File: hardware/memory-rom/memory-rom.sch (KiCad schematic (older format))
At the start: 26 parts, among them J1 Conn_Mem_Ext, J2 Conn_Power, U1 SST39VF040-70-4C-NHE, U2 74LVC1G86, U3 74LVC1G32, U4 74LVC1G332, U5 74LVC1G86, U6 MIC5504-3.3YM5

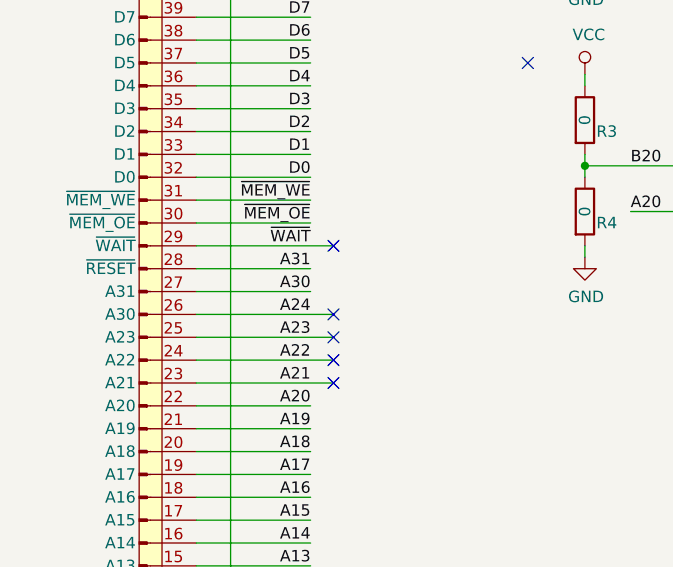
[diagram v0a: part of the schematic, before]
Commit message: Added ~RESET to memory bus
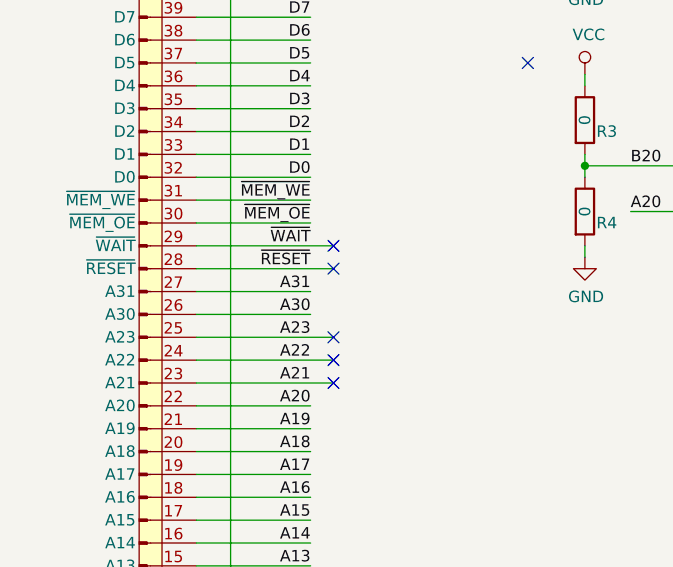
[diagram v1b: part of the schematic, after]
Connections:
- net A24 is gone; now on net A30: J1.26 (A30)
- net A30: no longer J1.27 (A31)
- net A31: now also J1.27 (A31); no longer J1.28 (~RESET)
- new net ~RESET: J1.28 (~RESET)
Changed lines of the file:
@@
 Text Label 1950 3800 2    50   ~ 0
 A23
-Text Label 1950 3700 2    50   ~ 0
-A24
 Text Label 1950 3400 2    50   ~ 0
 ~WAIT
@@
 Wire Wire Line
 	1950 4400 1450 4400
-Text Label 1950 3500 2    50   ~ 0
+Text Label 1950 3600 2    50   ~ 0
 A31
-Text Label 1950 3600 2    50   ~ 0
+Text Label 1950 3700 2    50   ~ 0
 A30
 Wire Wire Line
-	1950 3500 1450 3500
-Wire Wire Line
-	1450 3600 1950 3600
+	1950 3600 1450 3600
+Wire Wire Line
+	1450 3700 1950 3700
 $Comp
 L Mechanical:MountingHole H?
@@
 Connection ~ 1600 6200
 Wire Wire Line
-	1450 3700 2050 3700
+	1450 3500 2050 3500
 Wire Wire Line
 	1450 3800 2050 3800
@@
 Wire Wire Line
 	10100 3600 10100 3400
-NoConn ~ 2050 3700
+NoConn ~ 2050 3500
 NoConn ~ 2050 3800
 NoConn ~ 2050 3900
 NoConn ~ 2050 4000
+Text Label 1950 3500 2    50   ~ 0
+~RESET
 $EndSCHEMATC

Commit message: Unified footprints
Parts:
- D1: footprint LED_SMD:LED_0805_2012Metric -> LED_SMD:LED_0805_2012Metric_Pad1.15x1.40mm_HandSolder
- R1, R2, R3, R4, R5: footprint Resistor_SMD:R_0805_2012Metric -> Resistor_SMD:R_0805_2012Metric_Pad1.15x1.40mm_HandSolder
- U2, U3, U5, U6: footprint Package_TO_SOT_SMD:SOT-23-5 -> Package_TO_SOT_SMD:SOT-23-5_HandSoldering
- U4: footprint Package_TO_SOT_SMD:SOT-23-6 -> Package_TO_SOT_SMD:SOT-23-6_Handsoldering
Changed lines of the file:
@@
 F 0 "U4" H 6000 2333 50  0000 C CNN
 F 1 "74LVC1G332" H 6000 2424 50  0000 C CNN
-F 2 "Package_TO_SOT_SMD:SOT-23-6" H 5970 2620 50  0001 C CNN
+F 2 "Package_TO_SOT_SMD:SOT-23-6_Handsoldering" H 5970 2620 50  0001 C CNN
 F 3 "" H 5970 2620 50  0001 C CNN
 	1    6000 2650
@@
 F 0 "R1" H 3200 1500 50  0000 L CNN
 F 1 "0" V 3150 1550 50  0000 C CNN
-F 2 "Resistor_SMD:R_0805_2012Metric" V 3080 1550 50  0001 C CNN
+F 2 "Resistor_SMD:R_0805_2012Metric_Pad1.15x1.40mm_HandSolder" V 3080 1550 50  0001 C CNN
 F 3 "~" H 3150 1550 50  0001 C CNN
 	1    3150 1550
@@
 F 0 "R2" H 3200 1900 50  0000 L CNN
 F 1 "0" V 3150 1950 50  0000 C CNN
-F 2 "Resistor_SMD:R_0805_2012Metric" V 3080 1950 50  0001 C CNN
+F 2 "Resistor_SMD:R_0805_2012Metric_Pad1.15x1.40mm_HandSolder" V 3080 1950 50  0001 C CNN
 F 3 "~" H 3150 1950 50  0001 C CNN
 	1    3150 1950
@@
 F 0 "R3" H 3200 2800 50  0000 L CNN
 F 1 "0" V 3150 2850 50  0000 C CNN
-F 2 "Resistor_SMD:R_0805_2012Metric" V 3080 2850 50  0001 C CNN
+F 2 "Resistor_SMD:R_0805_2012Metric_Pad1.15x1.40mm_HandSolder" V 3080 2850 50  0001 C CNN
 F 3 "~" H 3150 2850 50  0001 C CNN
 	1    3150 2850
@@
 F 0 "R4" H 3200 3200 50  0000 L CNN
 F 1 "0" V 3150 3250 50  0000 C CNN
-F 2 "Resistor_SMD:R_0805_2012Metric" V 3080 3250 50  0001 C CNN
+F 2 "Resistor_SMD:R_0805_2012Metric_Pad1.15x1.40mm_HandSolder" V 3080 3250 50  0001 C CNN
 F 3 "~" H 3150 3250 50  0001 C CNN
 	1    3150 3250
@@
 F 0 "U3" H 4900 2875 50  0000 C CNN
 F 1 "74LVC1G32" H 4900 2784 50  0000 C CNN
-F 2 "Package_TO_SOT_SMD:SOT-23-5" H 4870 2520 50  0001 C CNN
+F 2 "Package_TO_SOT_SMD:SOT-23-5_HandSoldering" H 4870 2520 50  0001 C CNN
 F 3 "" H 4870 2520 50  0001 C CNN
 	1    4900 2550
@@
 F 0 "U5" H 3950 2833 50  0000 C CNN
 F 1 "74LVC1G86" H 3950 2924 50  0000 C CNN
-F 2 "Package_TO_SOT_SMD:SOT-23-5" H 3920 3120 50  0001 C CNN
+F 2 "Package_TO_SOT_SMD:SOT-23-5_HandSoldering" H 3920 3120 50  0001 C CNN
 F 3 "" H 3920 3120 50  0001 C CNN
 	1    3950 3150
@@
 F 0 "U2" H 3950 2175 50  0000 C CNN
 F 1 "74LVC1G86" H 3950 2084 50  0000 C CNN
-F 2 "Package_TO_SOT_SMD:SOT-23-5" H 3920 1820 50  0001 C CNN
+F 2 "Package_TO_SOT_SMD:SOT-23-5_HandSoldering" H 3920 1820 50  0001 C CNN
 F 3 "" H 3920 1820 50  0001 C CNN
 	1    3950 1850
@@
 F 0 "U6" H 7350 5967 50  0000 C CNN
 F 1 "MIC5504-3.3YM5" H 7350 5876 50  0000 C CNN
-F 2 "Package_TO_SOT_SMD:SOT-23-5" H 7350 5200 50  0001 C CNN
+F 2 "Package_TO_SOT_SMD:SOT-23-5_HandSoldering" H 7350 5200 50  0001 C CNN
 F 3 "http://ww1.microchip.com/downloads/en/DeviceDoc/MIC550X.pdf" H 7100 5850 50  0001 C CNN
 	1    7350 5600
@@
 F 0 "U2" H 3530 5846 50  0000 L CNN
 F 1 "74LVC1G86" H 3530 5755 50  0000 L CNN
-F 2 "Package_TO_SOT_SMD:SOT-23-5" H 3370 5770 50  0001 C CNN
+F 2 "Package_TO_SOT_SMD:SOT-23-5_HandSoldering" H 3370 5770 50  0001 C CNN
 F 3 "" H 3370 5770 50  0001 C CNN
 	2    3400 5800
@@
 F 0 "U5" H 4280 5846 50  0000 L CNN
 F 1 "74LVC1G86" H 4280 5755 50  0000 L CNN
-F 2 "Package_TO_SOT_SMD:SOT-23-5" H 4120 5770 50  0001 C CNN
+F 2 "Package_TO_SOT_SMD:SOT-23-5_HandSoldering" H 4120 5770 50  0001 C CNN
 F 3 "" H 4120 5770 50  0001 C CNN
 	2    4150 5800
@@
 F 0 "U3" H 5050 5900 50  0000 C CNN
 F 1 "74LVC1G32" H 5200 5800 50  0000 C CNN
-F 2 "Package_TO_SOT_SMD:SOT-23-5" H 4820 5770 50  0001 C CNN
+F 2 "Package_TO_SOT_SMD:SOT-23-5_HandSoldering" H 4820 5770 50  0001 C CNN
 F 3 "" H 4820 5770 50  0001 C CNN
 	2    4850 5800
@@
 F 0 "U4" H 2780 5846 50  0000 L CNN
 F 1 "74LVC1G332" H 2780 5755 50  0000 L CNN
-F 2 "Package_TO_SOT_SMD:SOT-23-6" H 2620 5770 50  0001 C CNN
+F 2 "Package_TO_SOT_SMD:SOT-23-6_Handsoldering" H 2620 5770 50  0001 C CNN
 F 3 "" H 2620 5770 50  0001 C CNN
 	2    2650 5800
@@
 F 0 "R5" H 10150 3200 50  0000 L CNN
 F 1 "330" V 10100 3250 50  0000 C CNN
-F 2 "Resistor_SMD:R_0805_2012Metric" V 10030 3250 50  0001 C CNN
+F 2 "Resistor_SMD:R_0805_2012Metric_Pad1.15x1.40mm_HandSolder" V 10030 3250 50  0001 C CNN
 F 3 "~" H 10100 3250 50  0001 C CNN
 	1    10100 3250
@@
 F 0 "D1" V 10138 2633 50  0000 R CNN
 F 1 "LED" V 10047 2633 50  0000 R CNN
-F 2 "LED_SMD:LED_0805_2012Metric" H 10100 2750 50  0001 C CNN
+F 2 "LED_SMD:LED_0805_2012Metric_Pad1.15x1.40mm_HandSolder" H 10100 2750 50  0001 C CNN
 F 3 "~" H 10100 2750 50  0001 C CNN
 	1    10100 2750

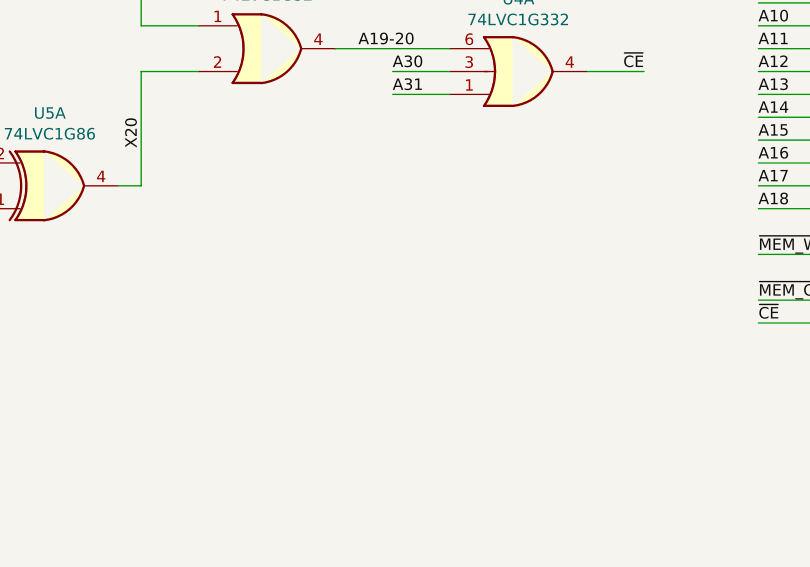
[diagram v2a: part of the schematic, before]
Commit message: Added test points
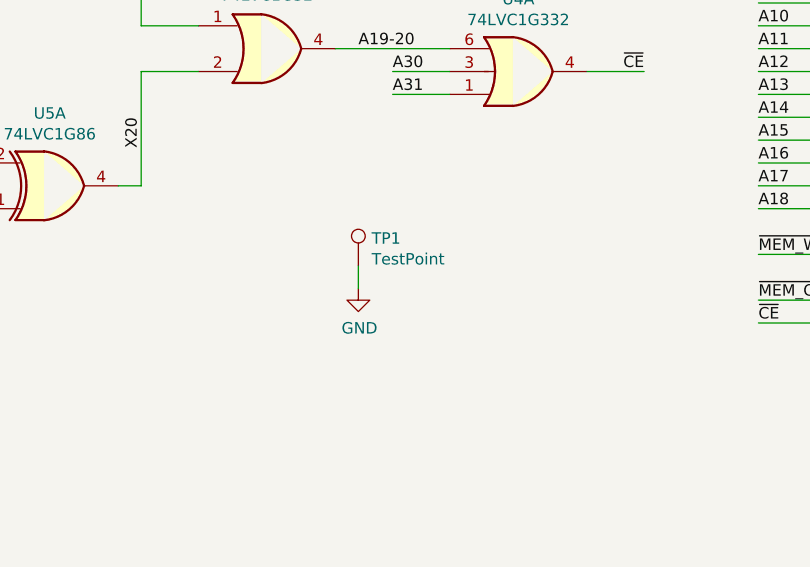
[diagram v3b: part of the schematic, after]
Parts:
- added TP1: TestPoint, TestPoint:TestPoint_THTPad_D2.0mm_Drill1.0mm, symbol Connector:TestPoint
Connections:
- net GND: now also TP1.1
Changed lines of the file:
@@
 P 8000 1150
 AR Path="/5EC6F875/5EC7A90A" Ref="#PWR?"  Part="1"
-AR Path="/5EC7A90A" Ref="#PWR01"  Part="1"
-F 0 "#PWR01" H 8000 1000 50  0001 C CNN
+AR Path="/5EC7A90A" Ref="#PWR?"  Part="1"
+F 0 "#PWR?" H 8000 1000 50  0001 C CNN
 F 1 "VCC" H 8017 1323 50  0000 C CNN
 F 2 "" H 8000 1150 50  0001 C CNN
@@
 P 8000 4050
 AR Path="/5EC6F875/5EC7A911" Ref="#PWR?"  Part="1"
-AR Path="/5EC7A911" Ref="#PWR07"  Part="1"
-F 0 "#PWR07" H 8000 3800 50  0001 C CNN
+AR Path="/5EC7A911" Ref="#PWR?"  Part="1"
+F 0 "#PWR?" H 8000 3800 50  0001 C CNN
 F 1 "GND" H 8005 3877 50  0000 C CNN
 F 2 "" H 8000 4050 50  0001 C CNN
@@
 P 1600 6300
 AR Path="/5ED0998A/5EC7A9C0" Ref="#PWR?"  Part="1"
-AR Path="/5EC7A9C0" Ref="#PWR012"  Part="1"
+AR Path="/5EC7A9C0" Ref="#PWR?"  Part="1"
 AR Path="/5EC6F875/5EC7A9C0" Ref="#PWR?"  Part="1"
-F 0 "#PWR012" H 1600 6050 50  0001 C CNN
+F 0 "#PWR?" H 1600 6050 50  0001 C CNN
 F 1 "GND" H 1605 6127 50  0000 C CNN
 F 2 "" H 1600 6300 50  0001 C CNN
@@
 P 3150 2150
 AR Path="/5EF37502/5EF44DEB" Ref="#PWR?"  Part="1"
-AR Path="/5EF44DEB" Ref="#PWR03"  Part="1"
-F 0 "#PWR03" H 3150 1900 50  0001 C CNN
+AR Path="/5EF44DEB" Ref="#PWR?"  Part="1"
+F 0 "#PWR?" H 3150 1900 50  0001 C CNN
 F 1 "GND" H 3155 1977 50  0000 C CNN
 F 2 "" H 3150 2150 50  0001 C CNN
@@
 P 3150 1350
 AR Path="/5EF37502/5EF44DF2" Ref="#PWR?"  Part="1"
-AR Path="/5EF44DF2" Ref="#PWR02"  Part="1"
-F 0 "#PWR02" H 3150 1200 50  0001 C CNN
+AR Path="/5EF44DF2" Ref="#PWR?"  Part="1"
+F 0 "#PWR?" H 3150 1200 50  0001 C CNN
 F 1 "VCC" H 3167 1523 50  0000 C CNN
 F 2 "" H 3150 1350 50  0001 C CNN
@@
 P 3150 3450
 AR Path="/5EF37502/5EF44E0D" Ref="#PWR?"  Part="1"
-AR Path="/5EF44E0D" Ref="#PWR06"  Part="1"
-F 0 "#PWR06" H 3150 3200 50  0001 C CNN
+AR Path="/5EF44E0D" Ref="#PWR?"  Part="1"
+F 0 "#PWR?" H 3150 3200 50  0001 C CNN
 F 1 "GND" H 3155 3277 50  0000 C CNN
 F 2 "" H 3150 3450 50  0001 C CNN
@@
 P 3150 2650
 AR Path="/5EF37502/5EF44E14" Ref="#PWR?"  Part="1"
-AR Path="/5EF44E14" Ref="#PWR05"  Part="1"
-F 0 "#PWR05" H 3150 2500 50  0001 C CNN
+AR Path="/5EF44E14" Ref="#PWR?"  Part="1"
+F 0 "#PWR?" H 3150 2500 50  0001 C CNN
 F 1 "VCC" H 3167 2823 50  0000 C CNN
 F 2 "" H 3150 2650 50  0001 C CNN
@@
 P 7900 5450
 AR Path="/5ED0998A/5EF4BF68" Ref="#PWR?"  Part="1"
-AR Path="/5EF4BF68" Ref="#PWR09"  Part="1"
+AR Path="/5EF4BF68" Ref="#PWR?"  Part="1"
 AR Path="/5EF37502/5EF4BF68" Ref="#PWR?"  Part="1"
-F 0 "#PWR09" H 7900 5300 50  0001 C CNN
+F 0 "#PWR?" H 7900 5300 50  0001 C CNN
 F 1 "VCC" H 7917 5623 50  0000 C CNN
 F 2 "" H 7900 5450 50  0001 C CNN
@@
 P 6150 6100
 AR Path="/5ED0998A/5EF4BF70" Ref="#PWR?"  Part="1"
-AR Path="/5EF4BF70" Ref="#PWR010"  Part="1"
+AR Path="/5EF4BF70" Ref="#PWR?"  Part="1"
 AR Path="/5EF37502/5EF4BF70" Ref="#PWR?"  Part="1"
-F 0 "#PWR010" H 6150 5850 50  0001 C CNN
+F 0 "#PWR?" H 6150 5850 50  0001 C CNN
 F 1 "GND" H 6155 5927 50  0000 C CNN
 F 2 "" H 6150 6100 50  0001 C CNN
@@
 P 7350 6100
 AR Path="/5ED0998A/5EF4BF87" Ref="#PWR?"  Part="1"
-AR Path="/5EF4BF87" Ref="#PWR011"  Part="1"
+AR Path="/5EF4BF87" Ref="#PWR?"  Part="1"
 AR Path="/5EF37502/5EF4BF87" Ref="#PWR?"  Part="1"
-F 0 "#PWR011" H 7350 5850 50  0001 C CNN
+F 0 "#PWR?" H 7350 5850 50  0001 C CNN
 F 1 "GND" H 7355 5927 50  0000 C CNN
 F 2 "" H 7350 6100 50  0001 C CNN
@@
 P 2650 6450
 AR Path="/5ED0998A/5EF4BFE0" Ref="#PWR?"  Part="1"
-AR Path="/5EF4BFE0" Ref="#PWR013"  Part="1"
+AR Path="/5EF4BFE0" Ref="#PWR?"  Part="1"
 AR Path="/5EF37502/5EF4BFE0" Ref="#PWR?"  Part="1"
-F 0 "#PWR013" H 2650 6200 50  0001 C CNN
+F 0 "#PWR?" H 2650 6200 50  0001 C CNN
 F 1 "GND" H 2655 6277 50  0000 C CNN
 F 2 "" H 2650 6450 50  0001 C CNN
@@
 P 2650 5150
 AR Path="/5ED0998A/5EF4BFE8" Ref="#PWR?"  Part="1"
-AR Path="/5EF4BFE8" Ref="#PWR08"  Part="1"
+AR Path="/5EF4BFE8" Ref="#PWR?"  Part="1"
 AR Path="/5EF37502/5EF4BFE8" Ref="#PWR?"  Part="1"
-F 0 "#PWR08" H 2650 5000 50  0001 C CNN
+F 0 "#PWR?" H 2650 5000 50  0001 C CNN
 F 1 "VCC" H 2667 5323 50  0000 C CNN
 F 2 "" H 2650 5150 50  0001 C CNN
@@
 P 6550 6100
 AR Path="/5EF37502/5EF4C00A" Ref="#FLG?"  Part="1"
-AR Path="/5EF4C00A" Ref="#FLG02"  Part="1"
-F 0 "#FLG02" H 6550 6175 50  0001 C CNN
+AR Path="/5EF4C00A" Ref="#FLG?"  Part="1"
+F 0 "#FLG?" H 6550 6175 50  0001 C CNN
 F 1 "PWR_FLAG" H 6550 6273 50  0000 C CNN
 F 2 "" H 6550 6100 50  0001 C CNN
@@
 P 6550 5400
 AR Path="/5EF37502/5EF4C013" Ref="#FLG?"  Part="1"
-AR Path="/5EF4C013" Ref="#FLG01"  Part="1"
-F 0 "#FLG01" H 6550 5475 50  0001 C CNN
+AR Path="/5EF4C013" Ref="#FLG?"  Part="1"
+F 0 "#FLG?" H 6550 5475 50  0001 C CNN
 F 1 "PWR_FLAG" H 6550 5574 50  0000 C CNN
 F 2 "" H 6550 5400 50  0001 C CNN
@@
 P 10100 2500
 AR Path="/5EF37502/5EF8DDFD" Ref="#PWR?"  Part="1"
-AR Path="/5EF8DDFD" Ref="#PWR04"  Part="1"
-F 0 "#PWR04" H 10100 2350 50  0001 C CNN
+AR Path="/5EF8DDFD" Ref="#PWR?"  Part="1"
+F 0 "#PWR?" H 10100 2350 50  0001 C CNN
 F 1 "VCC" H 10117 2673 50  0000 C CNN
 F 2 "" H 10100 2500 50  0001 C CNN
@@
 Text Label 1950 3500 2    50   ~ 0
 ~RESET
+$Comp
+L Connector:TestPoint TP1
+U 1 1 5F064DFA
+P 5300 3500
+F 0 "TP1" H 5358 3620 50  0000 L CNN
+F 1 "TestPoint" H 5358 3529 50  0000 L CNN
+F 2 "TestPoint:TestPoint_THTPad_D2.0mm_Drill1.0mm" H 5500 3500 50  0001 C CNN
+F 3 "~" H 5500 3500 50  0001 C CNN
+	1    5300 3500
+	1    0    0    -1
+$EndComp
+$Comp
+L power:GND #PWR?
+U 1 1 5F064E5C
+P 5300 3600
+AR Path="/5EC6F875/5F064E5C" Ref="#PWR?"  Part="1"
+AR Path="/5F064E5C" Ref="#PWR?"  Part="1"
+F 0 "#PWR?" H 5300 3350 50  0001 C CNN
+F 1 "GND" H 5305 3427 50  0000 C CNN
+F 2 "" H 5300 3600 50  0001 C CNN
+F 3 "" H 5300 3600 50  0001 C CNN
+	1    5300 3600
+	1    0    0    -1
+$EndComp
+Wire Wire Line
+	5300 3500 5300 3600
 $EndSCHEMATC

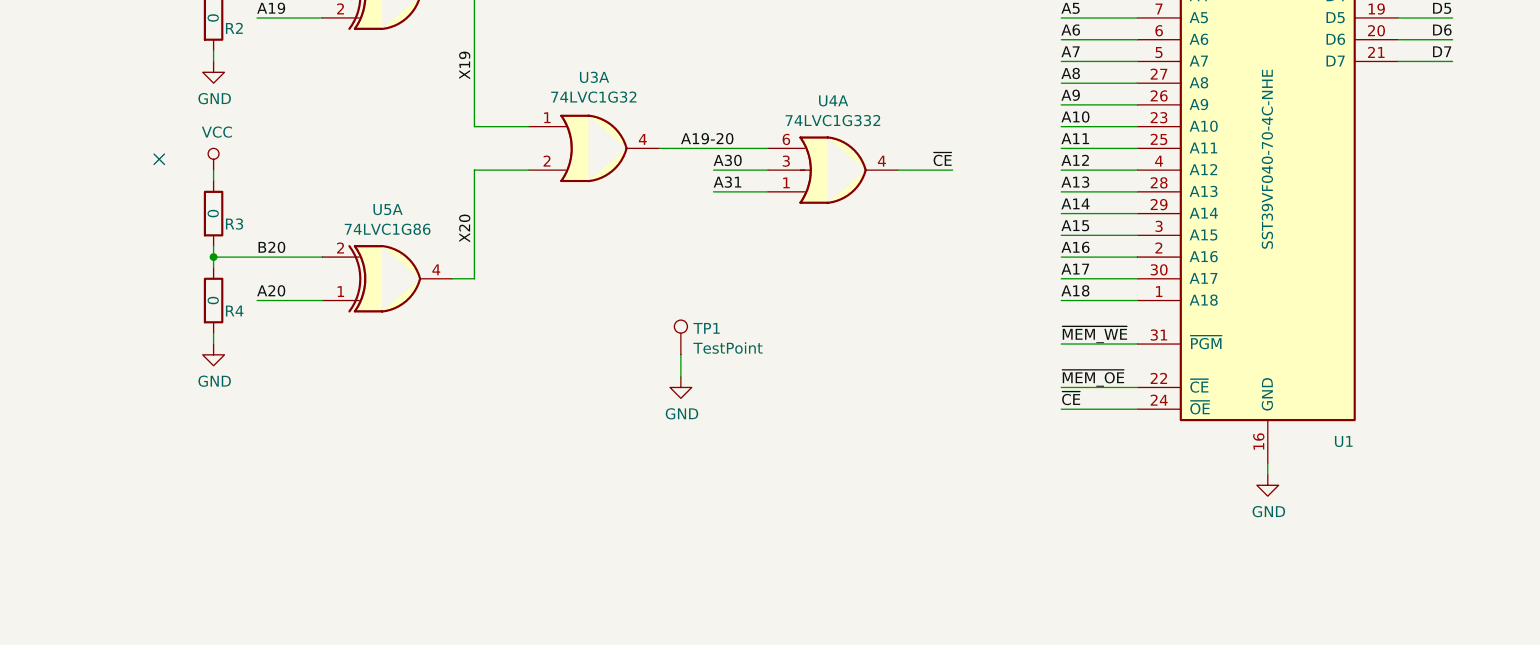
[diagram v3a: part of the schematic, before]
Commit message: Added errata to ROM schematic
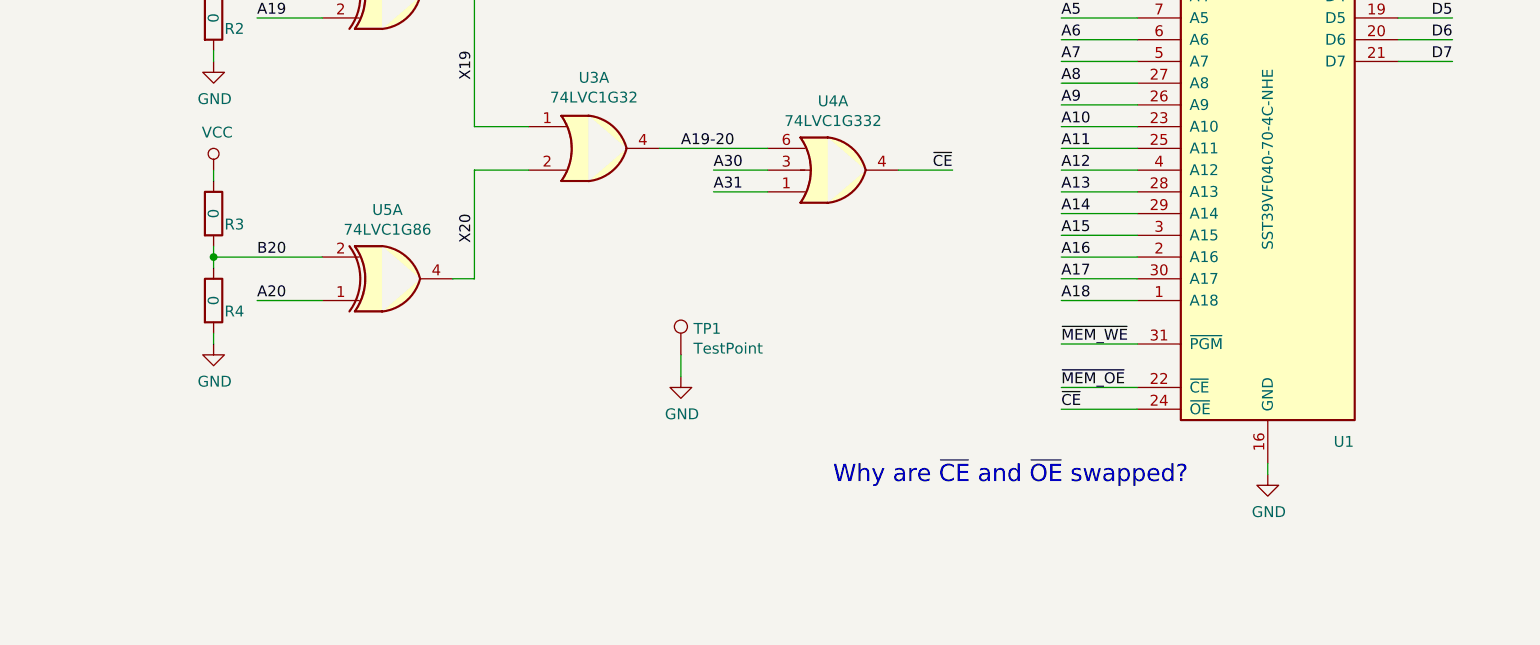
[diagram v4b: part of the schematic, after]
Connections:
- no-connect marks 6 -> 5
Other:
- note added: "Why are ~CE~ and ~OE~ swapped?"
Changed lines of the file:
@@
 EESchema Schematic File Version 4
-LIBS:memory-rom-cache
-EELAYER 26 0
+EELAYER 30 0
 EELAYER END
 $Descr A4 11693 8268
@@
 	1450 3400 2050 3400
 NoConn ~ 2050 3400
-NoConn ~ 2900 2600
 $Comp
 L riscv-serial:Conn_Mem_Ext J1
@@
 Wire Wire Line
 	5300 3500 5300 3600
+Text Notes 6000 4100 0    79   ~ 0
+Why are ~CE~ and ~OE~ swapped?
 $EndSCHEMATC
